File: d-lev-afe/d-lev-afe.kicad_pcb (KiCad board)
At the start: 4 copper layers, 89 x 50 mm, 36 parts, among them J1 S8B-PH-SM4-TB, Q1 MMBT3904, Q2 MMBT3906, U1 74AHC04, U2 AP2112K-3.3, U3 SRV05-4

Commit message: drc improvements
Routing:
- net GND: track 29.9 -> 28.4 mm, vias 16 -> 17
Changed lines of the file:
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@@
   (segment (start 166.191737 88.893389) (end 166.3 88.785126) (width 0.4) (layer "F.Cu") (net 2))
   (segment (start 169.279849 97.493437) (end 169.278898 97.494388) (width 0.4) (layer "F.Cu") (net 2))
-  (segment (start 163.025 95.27) (end 164.43 95.27) (width 0.4) (layer "F.Cu") (net 2))
   (segment (start 166.3 87.607626) (end 166.303813 87.603813) (width 0.4) (layer "F.Cu") (net 2))
   (segment (start 166.3 88.1) (end 166.469835 88.269835) (width 0.4) (layer "F.Cu") (net 2))
@@
   (segment (start 146.6 96) (end 149.15 96) (width 0.4) (layer "F.Cu") (net 2))
   (segment (start 155.950001 105.649999) (end 156.3 105.3) (width 0.4) (layer "F.Cu") (net 2))
-  (segment (start 164.43 95.27) (end 164.5 95.2) (width 0.4) (layer "F.Cu") (net 2))
   (segment (start 163.7526 99.6188) (end 165.1366 99.6188) (width 0.4) (layer "F.Cu") (net 2))
   (segment (start 162.7938 99.6188) (end 162.575 99.4) (width 0.4) (layer "F.Cu") (net 2))
@@
   (via (at 155.2 100.633334) (size 0.6) (drill 0.3) (layers "F.Cu" "B.Cu") (free) (net 2))
   (via (at 146.6 96) (size 0.6) (drill 0.3) (layers "F.Cu" "B.Cu") (net 2))
-  (via (at 164.5 95.2) (size 0.6) (drill 0.3) (layers "F.Cu" "B.Cu") (net 2))
+  (via (at 165.8 94) (size 0.6) (drill 0.3) (layers "F.Cu" "B.Cu") (free) (net 2))
   (via (at 167.101935 88.269835) (size 0.6) (drill 0.3) (layers "F.Cu" "B.Cu") (free) (net 2))
   (via (at 151.7396 92.0098) (size 0.6) (drill 0.3) (layers "F.Cu" "B.Cu") (net 2))
@@
   (via (at 146.6 92) (size 0.6) (drill 0.3) (layers "F.Cu" "B.Cu") (net 2))
   (via (at 155.2 99.5) (size 0.6) (drill 0.3) (layers "F.Cu" "B.Cu") (free) (net 2))
+  (via (at 169 88.2) (size 0.6) (drill 0.3) (layers "F.Cu" "B.Cu") (free) (net 2))
   (arc (start 161.374955 90.1954) (mid 161.371427 90.196101) (end 161.368437 90.1981) (width 0.4) (layer "F.Cu") (net 2))
   (arc (start 169.279849 97.493437) (mid 169.280552 97.492383) (end 169.2808 97.491141) (width 0.4) (layer "F.Cu") (net 2))

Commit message: everything passes drc as much as i care for it to, added silk art
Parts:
- added G***: LOGO, LOGO, B.Cu at (212.3, 97.5)

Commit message: Add JLC releases
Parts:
- moved AE1 132.2 mm to (61.8, 25.9)
- moved AE2 132.2 mm to (61.8, 51.0)
- moved C10 132.2 mm to (48.3, 47.5)
- moved C2 132.2 mm to (37.5, 42.9)
- moved C5 132.2 mm to (33.9, 46.3)
- moved C7 132.2 mm to (42.3, 42.8)
- moved C8 132.2 mm to (48.3, 45.4)
- moved G*** 132.2 mm to (92.8, 40.9)
- moved H1 132.2 mm to (23.5, 23.5)
- moved H2 132.2 mm to (92.5, 23.5)
- moved H3 132.2 mm to (23.5, 53.5)
- moved H4 132.2 mm to (61.8, 38.5)
- moved H5 132.2 mm to (92.5, 53.5)
- moved J1 132.2 mm to (26.8, 38.4)
- moved L2 132.2 mm to (89.6, 45.1)
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
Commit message: Add iBOMs and additional part numbers
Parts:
- C1, C7: value 0.1uF -> 100n
- C10: value 1p -> 2.4p
- C2: value .1u -> 100n
- R6: value 220K -> 220k

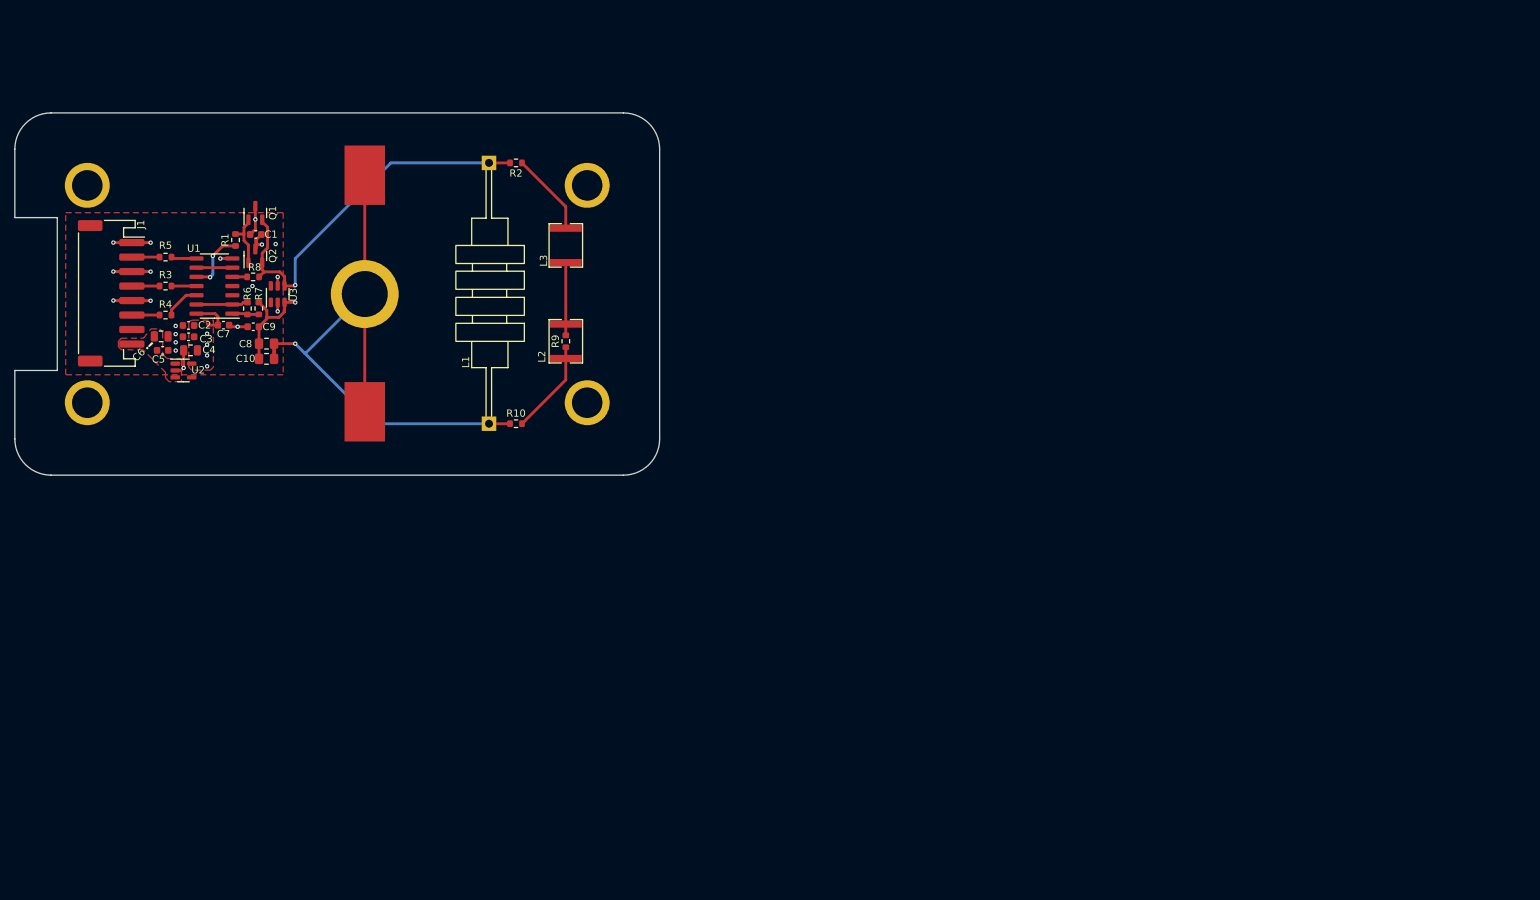
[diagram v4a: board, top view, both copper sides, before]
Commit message: d-lev-afe: switch to 2 layers, add 'antenna' version, pick out JLC parts
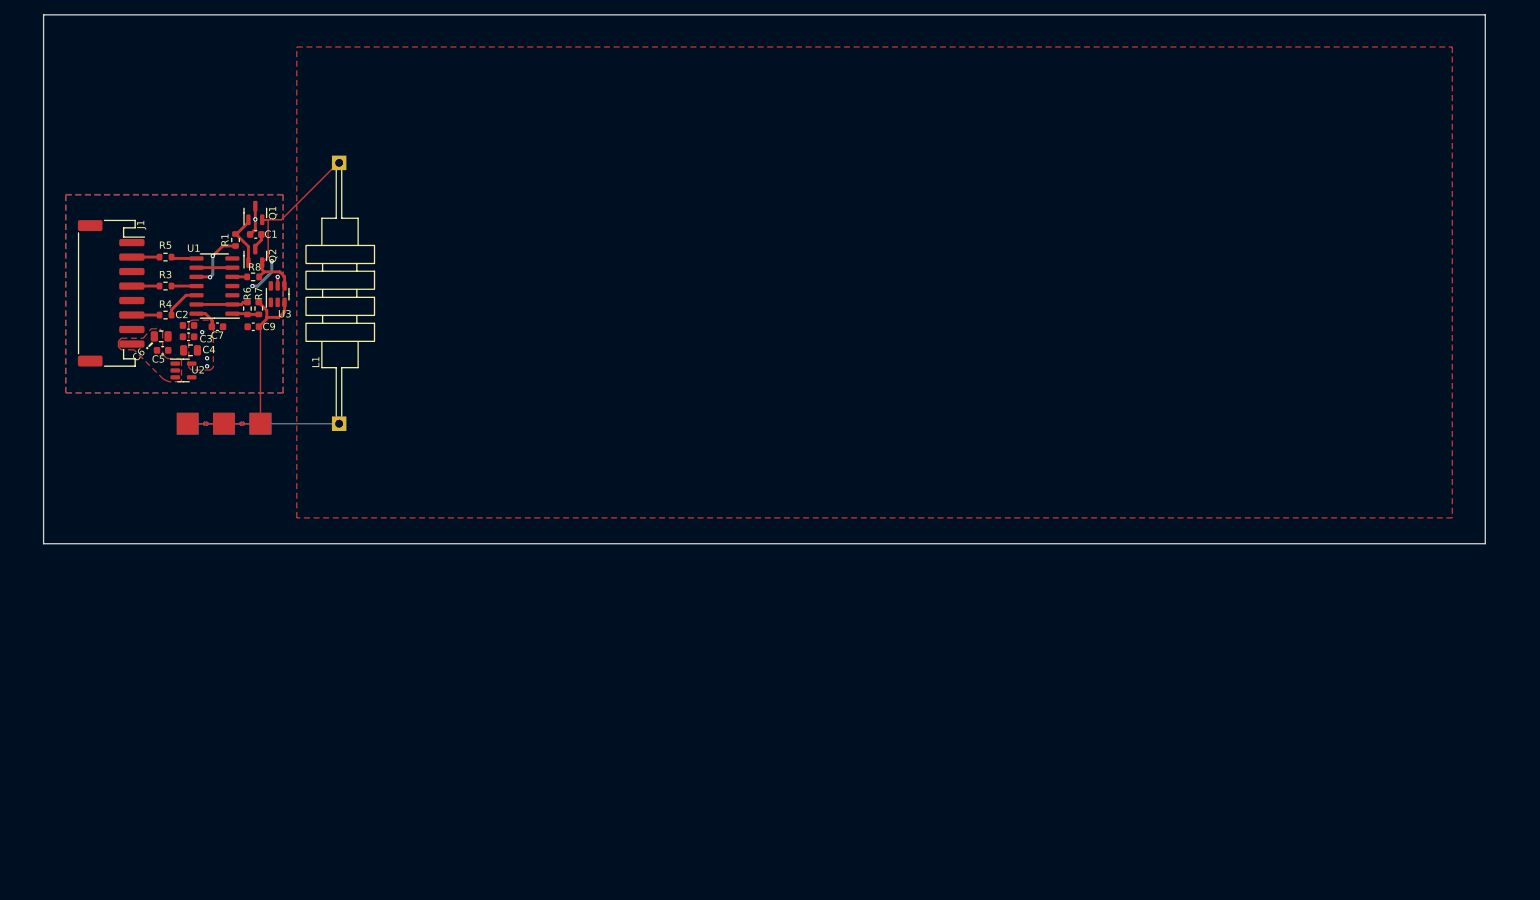
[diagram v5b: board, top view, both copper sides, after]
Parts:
- removed AE1, AE2: PLATE, theremin:keystone-PN5331TR
- removed G***: LOGO, LOGO
- removed H1, H2, H3, H5: Standoff_2, theremin:SMTSO-M3
- removed H4: Standoff_1, theremin:SMTSO-M4
- removed L2, L3: 1m, theremin:Coilcraft_DO1605T
- removed R10, R2, R9: 0, Resistor_SMD:R_0603_1608Metric
- added C11: 1pF, theremin:testpoint_cap_1pf, F.Cu at (37.4, 56.4)
- added JP1: SolderJumper_2_Open, theremin:SolderJumper-0.5mm-Tiny, F.Cu at (44.9, 56.4)
- added JP2: SolderJumper_2_Open, theremin:SolderJumper-0.5mm-Tiny, B.Cu at (44.9, 56.4)
- added JP3: SolderJumper_2_Open, theremin:SolderJumper-0.5mm-Tiny, B.Cu at (39.9, 56.4)
- added JP4: SolderJumper_2_Open, theremin:SolderJumper-0.5mm-Tiny, F.Cu at (39.9, 56.4)
- C10: value 2.4p -> 1pF; footprint Capacitor_SMD:C_0805_2012Metric_Pad1.18x1.45mm_HandSolder -> theremin:testpoint_cap_1pf
- C8: value 1p -> 1pF; footprint Capacitor_SMD:C_0805_2012Metric_Pad1.18x1.45mm_HandSolder -> theremin:testpoint_cap_1pf
- U2: value AP2112K-3.3 -> HT7833-2
- moved L1 20.7 mm to (58.3, 38.4)
- moved C8 11.1 mm to (47.4, 56.4), turned to 0 degrees
- moved C10 10.7 mm to (42.4, 56.4), turned to 0 degrees
- moved C7 0.86 mm to (41.5, 43.0)
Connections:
- C10 pad 1: L_IN -> Net-(JP1-B)
- C10 pad 2: /C_DIV -> Net-(JP2-B)
- C8 pad 1: L_IN -> /C_DIV
- C8 pad 2: /C_DIV -> L_IN
- J1 pad MP1: unconnected-(J1-MountPin1-PadMP1) -> GND
- J1 pad MP2: unconnected-(J1-MountPin2-PadMP2) -> GND
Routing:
- net L_IN: track 85.7 -> 13.1 mm, vias 1 -> 0
- net L_OUT: track 53.6 -> 27.7 mm, vias 1 -> 0
- net GND: track 28.4 -> 7.33 mm, vias 17 -> 2
- net Net-(L2-Pad1): track 13.1 -> 0.00 mm
- net Net-(L3-Pad2): track 11.5 -> 0.00 mm
- net Net-(L2-Pad2): track 10.0 -> 0.00 mm
- net /C_DIV: track 14.3 -> 24.0 mm, vias 1 -> 0
- net Net-(JP2-B): track 0.00 -> 4.42 mm
- net Net-(JP1-B): track 0.00 -> 4.42 mm
- net +3V3: track 11.3 -> 8.85 mm, vias 6 -> 5
- net Net-(JP4-B): track 0.00 -> 2.20 mm
- net Net-(JP3-B): track 0.00 -> 2.20 mm
- added copper zone on B.Cu, net +3V3
- added copper zone on F.Cu, net L_IN
- removed copper zone on In2.Cu, net +3V3
- removed copper zone on In1.Cu, net GND
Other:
- board size 89 x 50 mm -> 199 x 73 mm
- copper layers 4 -> 2

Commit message: pushed smaller AFE board
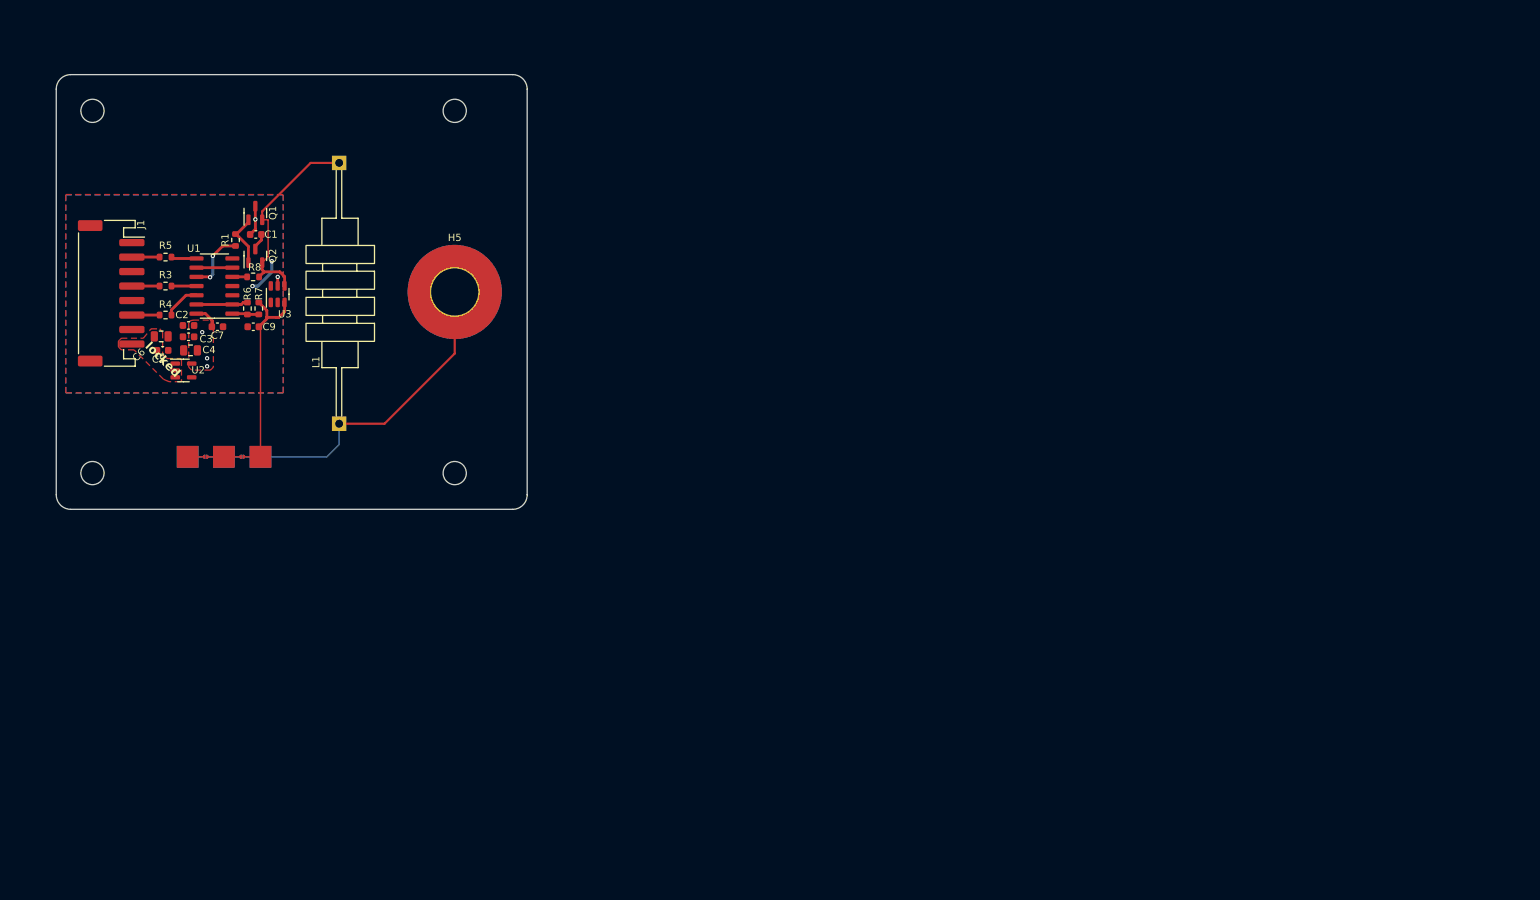
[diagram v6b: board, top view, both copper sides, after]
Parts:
- added H1: MountingHole, MountingHole:MountingHole_3.2mm_M3, F.Cu at (74.2, 13.2)
- added H2: MountingHole, MountingHole:MountingHole_3.2mm_M3, F.Cu at (24.2, 13.2)
- added H3: MountingHole, MountingHole:MountingHole_3.2mm_M3, F.Cu at (24.2, 63.2)
- added H4: MountingHole, MountingHole:MountingHole_3.2mm_M3, F.Cu at (74.2, 63.2)
- added H5: MountingHole_Pad, MountingHole:MountingHole_6.5mm_Pad_TopBottom, F.Cu at (74.2, 38.2)
- moved C10 4.56 mm to (42.4, 61.0)
- moved C11 4.56 mm to (37.4, 61.0)
- moved C8 4.56 mm to (47.4, 61.0)
- moved JP1 4.56 mm to (44.9, 61.0)
- moved JP2 4.56 mm to (44.9, 61.0)
- moved JP3 4.56 mm to (39.9, 61.0)
- moved JP4 4.56 mm to (39.9, 61.0)
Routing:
- net L_IN: track 13.1 -> 45.1 mm
- net /C_DIV: track 24.0 -> 28.6 mm
- net L_OUT: track 27.7 -> 28.4 mm
- removed copper zone on F.Cu, net L_IN
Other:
- board size 199 x 73 mm -> 65 x 60 mm
- board text added: "6.5mm ID hole in middle"
- board text added: "locked"
- board text removed: "!"
